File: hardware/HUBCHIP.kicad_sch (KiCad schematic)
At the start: 44 parts, among them U13 USB5926C, X1 ECS-2033-250-BN

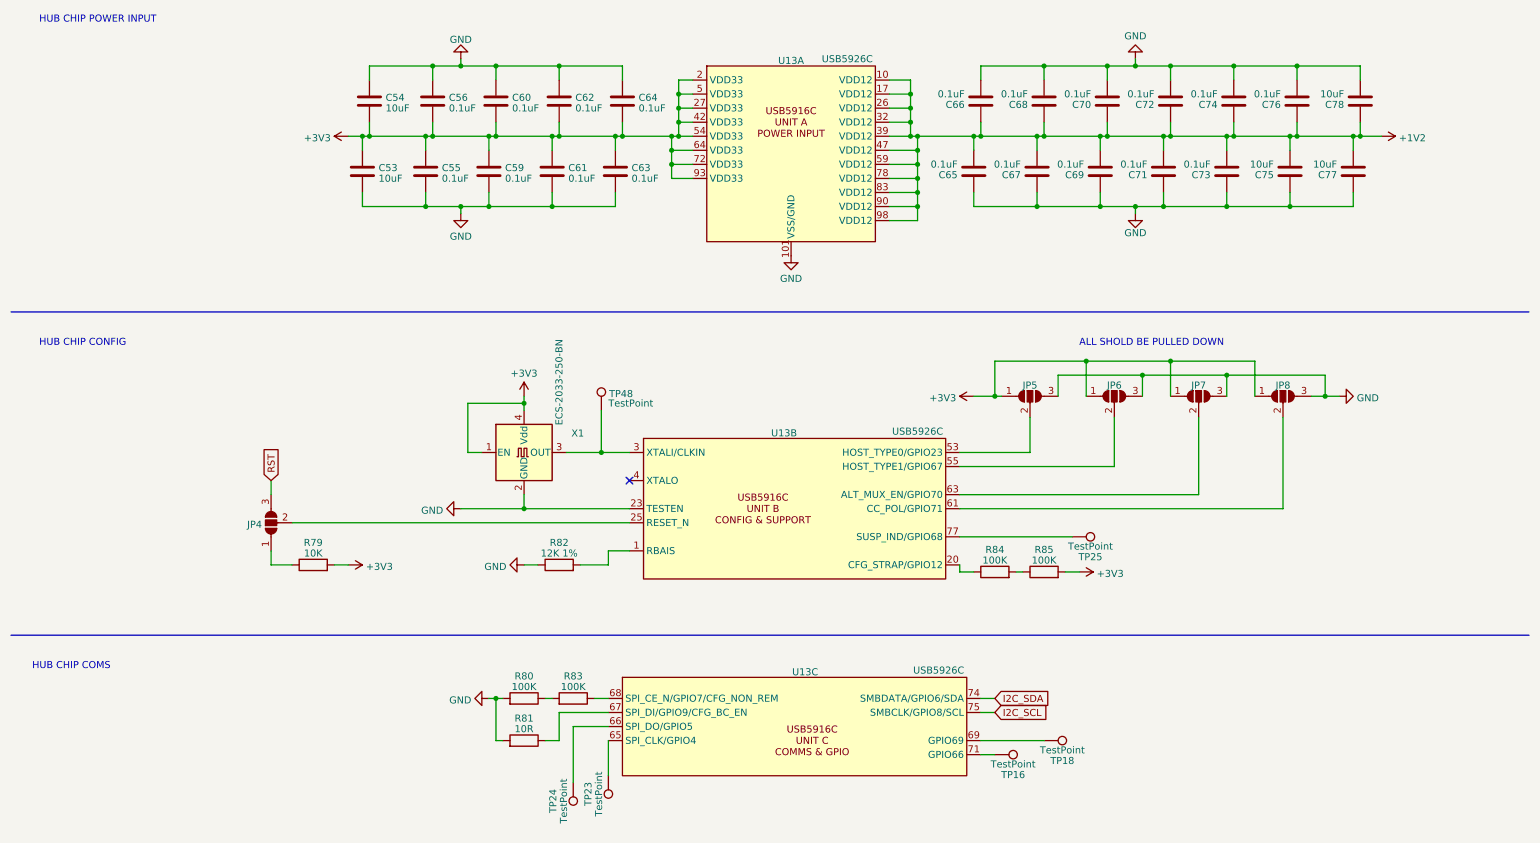
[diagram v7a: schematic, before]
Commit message: migrated to the esp32-s2 and starting new board revison
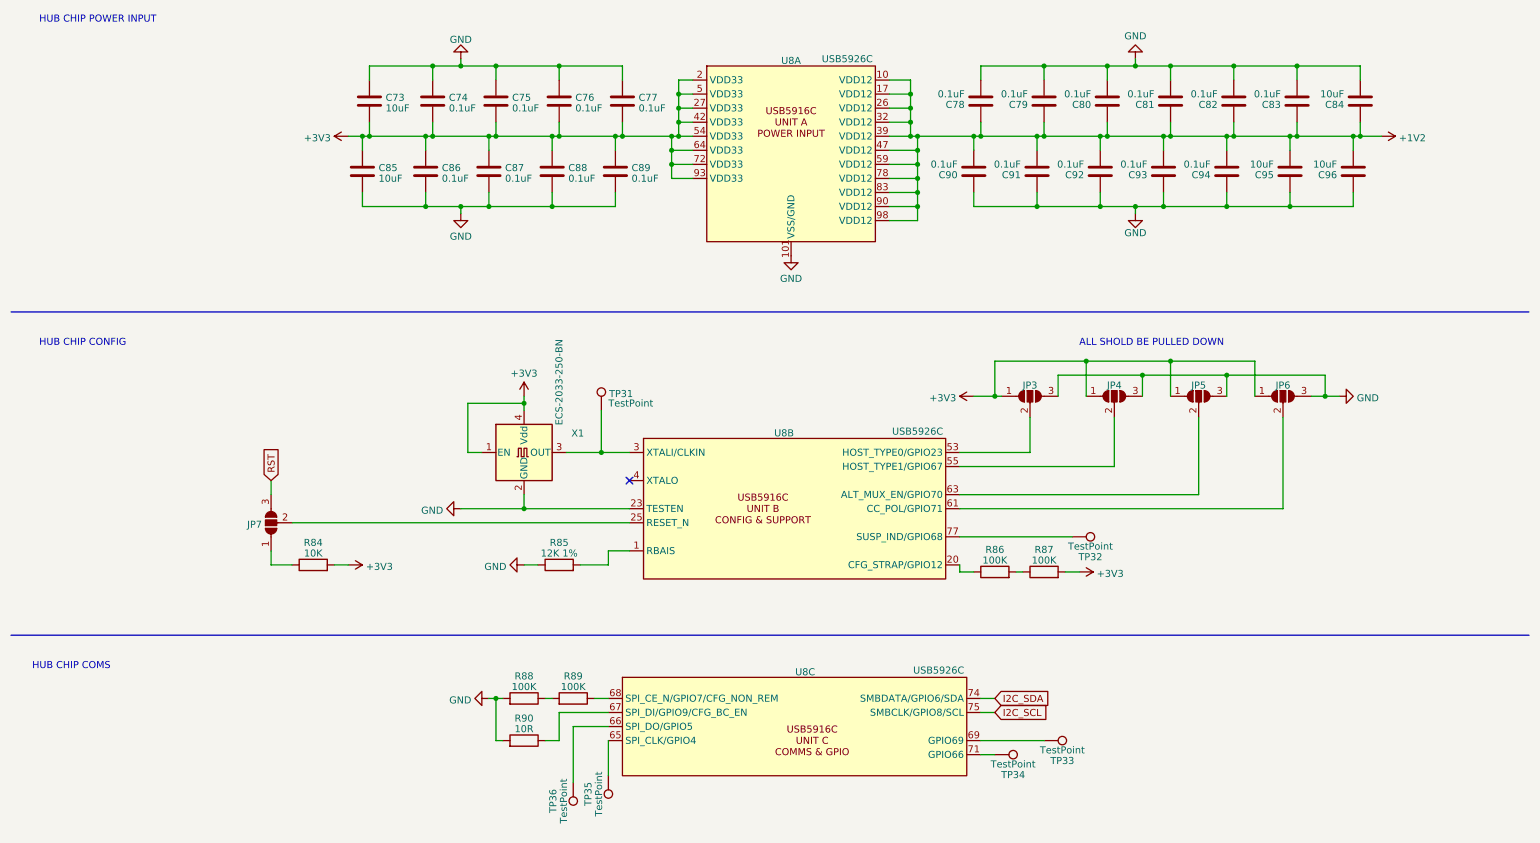
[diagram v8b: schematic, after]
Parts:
- renumbered C54 to C73, C56 to C74, C60 to C75, C62 to C76, C64 to C77, C66 to C78, C68 to C79, C70 to C80, C72 to C81, C74 to C82, C76 to C83, C78 to C84, C53 to C85, C55 to C86, C59 to C87, C61 to C88, C63 to C89, C65 to C90, C67 to C91, C69 to C92, C71 to C93, C73 to C94, C75 to C95, C77 to C96, JP5 to JP3, JP6 to JP4, JP7 to JP5, JP8 to JP6, JP4 to JP7, R79 to R84, R82 to R85, R84 to R86, R85 to R87, R80 to R88, R83 to R89, R81 to R90, TP48 to TP31, TP25 to TP32, TP18 to TP33, TP16 to TP34, TP23 to TP35, TP24 to TP36, U13 to U8
